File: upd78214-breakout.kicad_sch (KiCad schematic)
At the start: 1 part

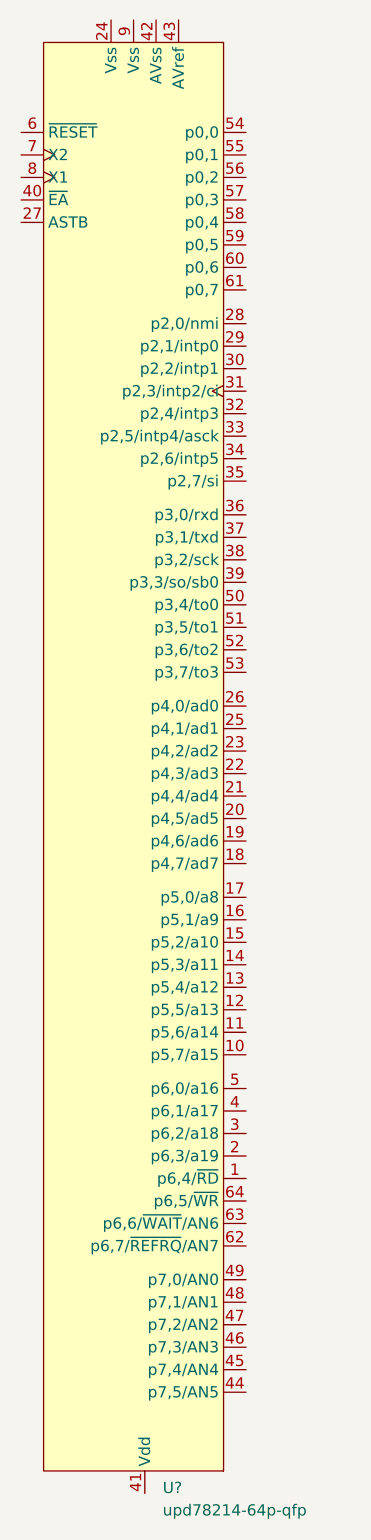
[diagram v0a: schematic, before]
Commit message: Fix VSS/VDD confusion
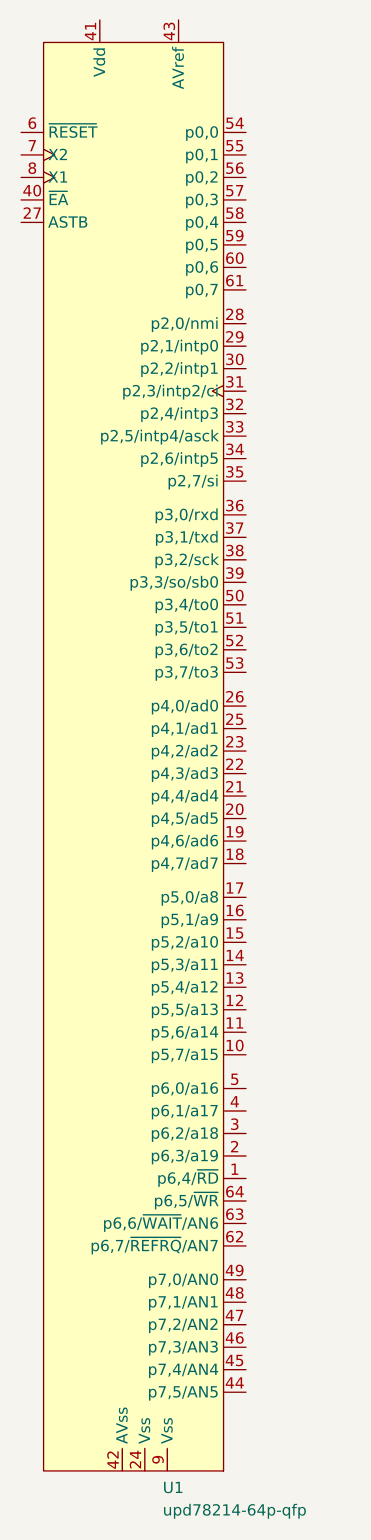
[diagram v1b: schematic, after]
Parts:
- gave numbers to parts that had none: 1
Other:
- moved on the sheet: U1
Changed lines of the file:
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@@
   (symbol (lib_id "NEC:upd78214-64p-qfp") (at 121.285 26.035 0) (unit 1)
     (in_bom yes) (on_board yes) (fields_autoplaced)
-    (property "Reference" "U?" (id 0) (at 123.3044 187.96 0)
+    (property "Reference" "U1" (id 0) (at 123.3044 187.96 0)
       (effects (font (size 1.27 1.27)) (justify left))
     )
@@
   (symbol_instances
     (path "/69c7afce-fa24-4138-9624-1d45a5afe81a"
-      (reference "U?") (unit 1) (value "upd78214-64p-qfp") (footprint "Package_QFP:TQFP-64_14x14mm_P0.8mm")
+      (reference "U1") (unit 1) (value "upd78214-64p-qfp") (footprint "Package_QFP:TQFP-64_14x14mm_P0.8mm")
     )
   )

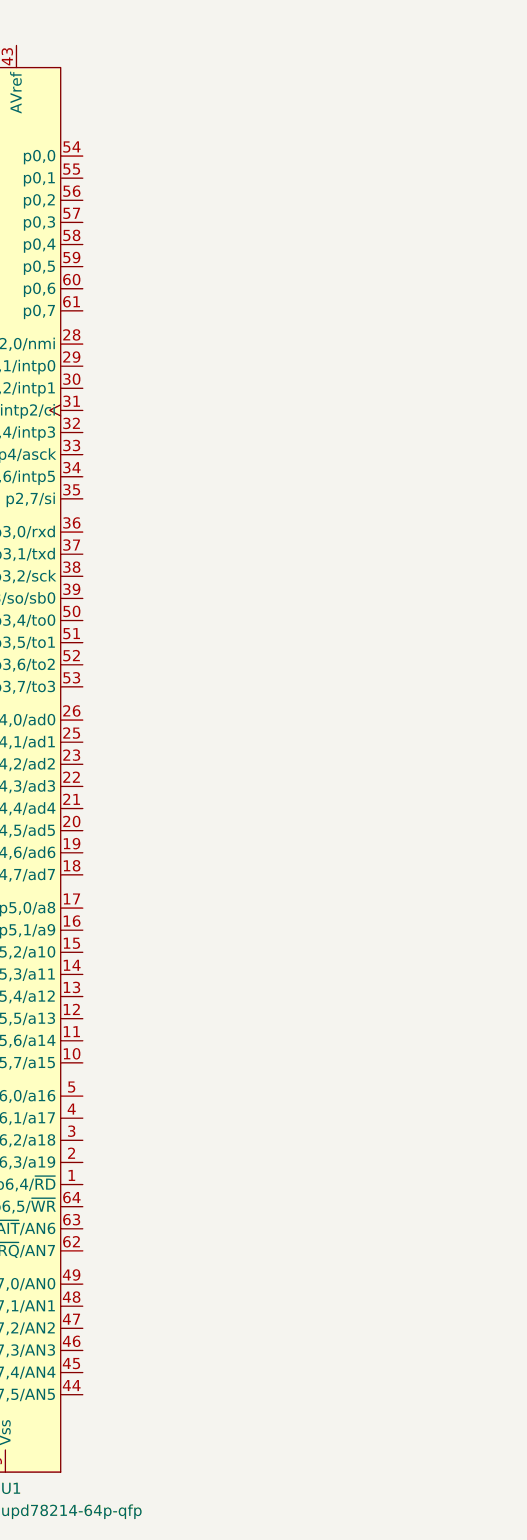
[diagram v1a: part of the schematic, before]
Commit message: NEC footprint, Toshiba symbol
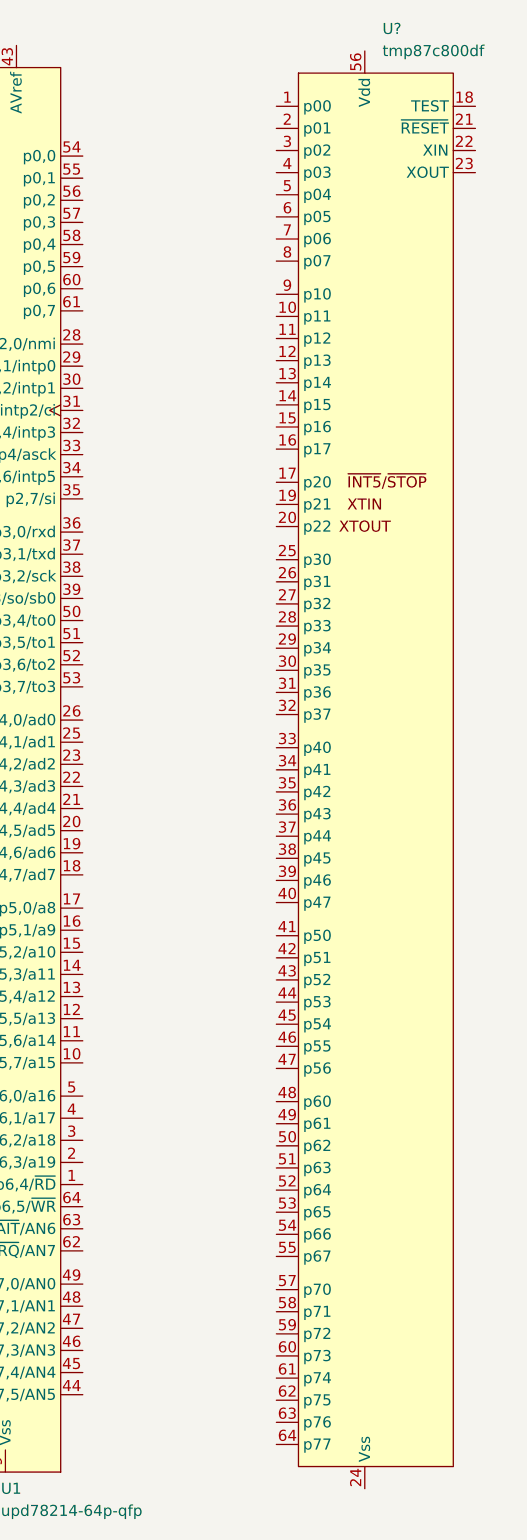
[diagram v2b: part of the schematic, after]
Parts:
- added U?: tmp87c800df, symbol Toshiba:tmp87c800df
- U1: footprint Package_QFP:TQFP-64_14x14mm_P0.8mm -> NEC:QFP-64_14x14_Pitch0.8mm
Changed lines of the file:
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@@
       (effects (font (size 1.27 1.27)) (justify left))
     )
-    (property "Footprint" "Package_QFP:TQFP-64_14x14mm_P0.8mm" (id 2) (at 121.285 26.035 0)
+    (property "Footprint" "NEC:QFP-64_14x14_Pitch0.8mm" (id 2) (at 121.285 26.035 0)
       (effects (font (size 1.27 1.27)) hide)
     )
     (property "Datasheet" "" (id 3) (at 121.285 26.035 0)
+      (effects (font (size 1.27 1.27)) hide)
+    )
+    (pin "1")
+    (pin "10")
+    (pin "11")
+    (pin "12")
+    (pin "13")
+    (pin "14")
+    (pin "15")
+    (pin "16")
+    (pin "17")
+    (pin "18")
+    (pin "19")
+    (pin "2")
+    (pin "20")
+    (pin "21")
+    (pin "22")
+    (pin "23")
+    (pin "24")
+    (pin "25")
+    (pin "26")
+    (pin "27")
+    (pin "28")
+    (pin "29")
+    (pin "3")
+    (pin "30")
+    (pin "31")
+    (pin "32")
+    (pin "33")
+    (pin "34")
+    (pin "35")
+    (pin "36")
+    (pin "37")
+    (pin "38")
+    (pin "39")
+    (pin "4")
+    (pin "40")
+    (pin "41")
+    (pin "42")
+    (pin "43")
+    (pin "44")
+    (pin "45")
+    (pin "46")
+    (pin "47")
+    (pin "48")
+    (pin "49")
+    (pin "5")
+    (pin "50")
+    (pin "51")
+    (pin "52")
+    (pin "53")
+    (pin "54")
+    (pin "55")
+    (pin "56")
+    (pin "57")
+    (pin "58")
+    (pin "59")
+    (pin "6")
+    (pin "60")
+    (pin "61")
+    (pin "62")
+    (pin "63")
+    (pin "64")
+    (pin "7")
+    (pin "8")
+    (pin "9")
+  )
+  (symbol (lib_id "Toshiba:tmp87c800df") (at 170.18 38.1 0) (unit 1)
+    (in_bom yes) (on_board yes) (fields_autoplaced)
+    (property "Reference" "U?" (id 0) (at 167.1194 20.32 0)
+      (effects (font (size 1.27 1.27)) (justify left))
+    )
+    (property "Value" "tmp87c800df" (id 1) (at 167.1194 22.86 0)
+      (effects (font (size 1.27 1.27)) (justify left))
+    )
+    (property "Footprint" "" (id 2) (at 170.18 38.1 0)
+      (effects (font (size 1.27 1.27)) hide)
+    )
+    (property "Datasheet" "" (id 3) (at 170.18 38.1 0)
       (effects (font (size 1.27 1.27)) hide)
     )
@@
   (symbol_instances
     (path "/69c7afce-fa24-4138-9624-1d45a5afe81a"
-      (reference "U1") (unit 1) (value "upd78214-64p-qfp") (footprint "Package_QFP:TQFP-64_14x14mm_P0.8mm")
+      (reference "U1") (unit 1) (value "upd78214-64p-qfp") (footprint "NEC:QFP-64_14x14_Pitch0.8mm")
+    )
+    (path "/d24b5999-bb41-4238-a79a-8ddf5d237a80"
+      (reference "U?") (unit 1) (value "tmp87c800df") (footprint "")
     )
   )

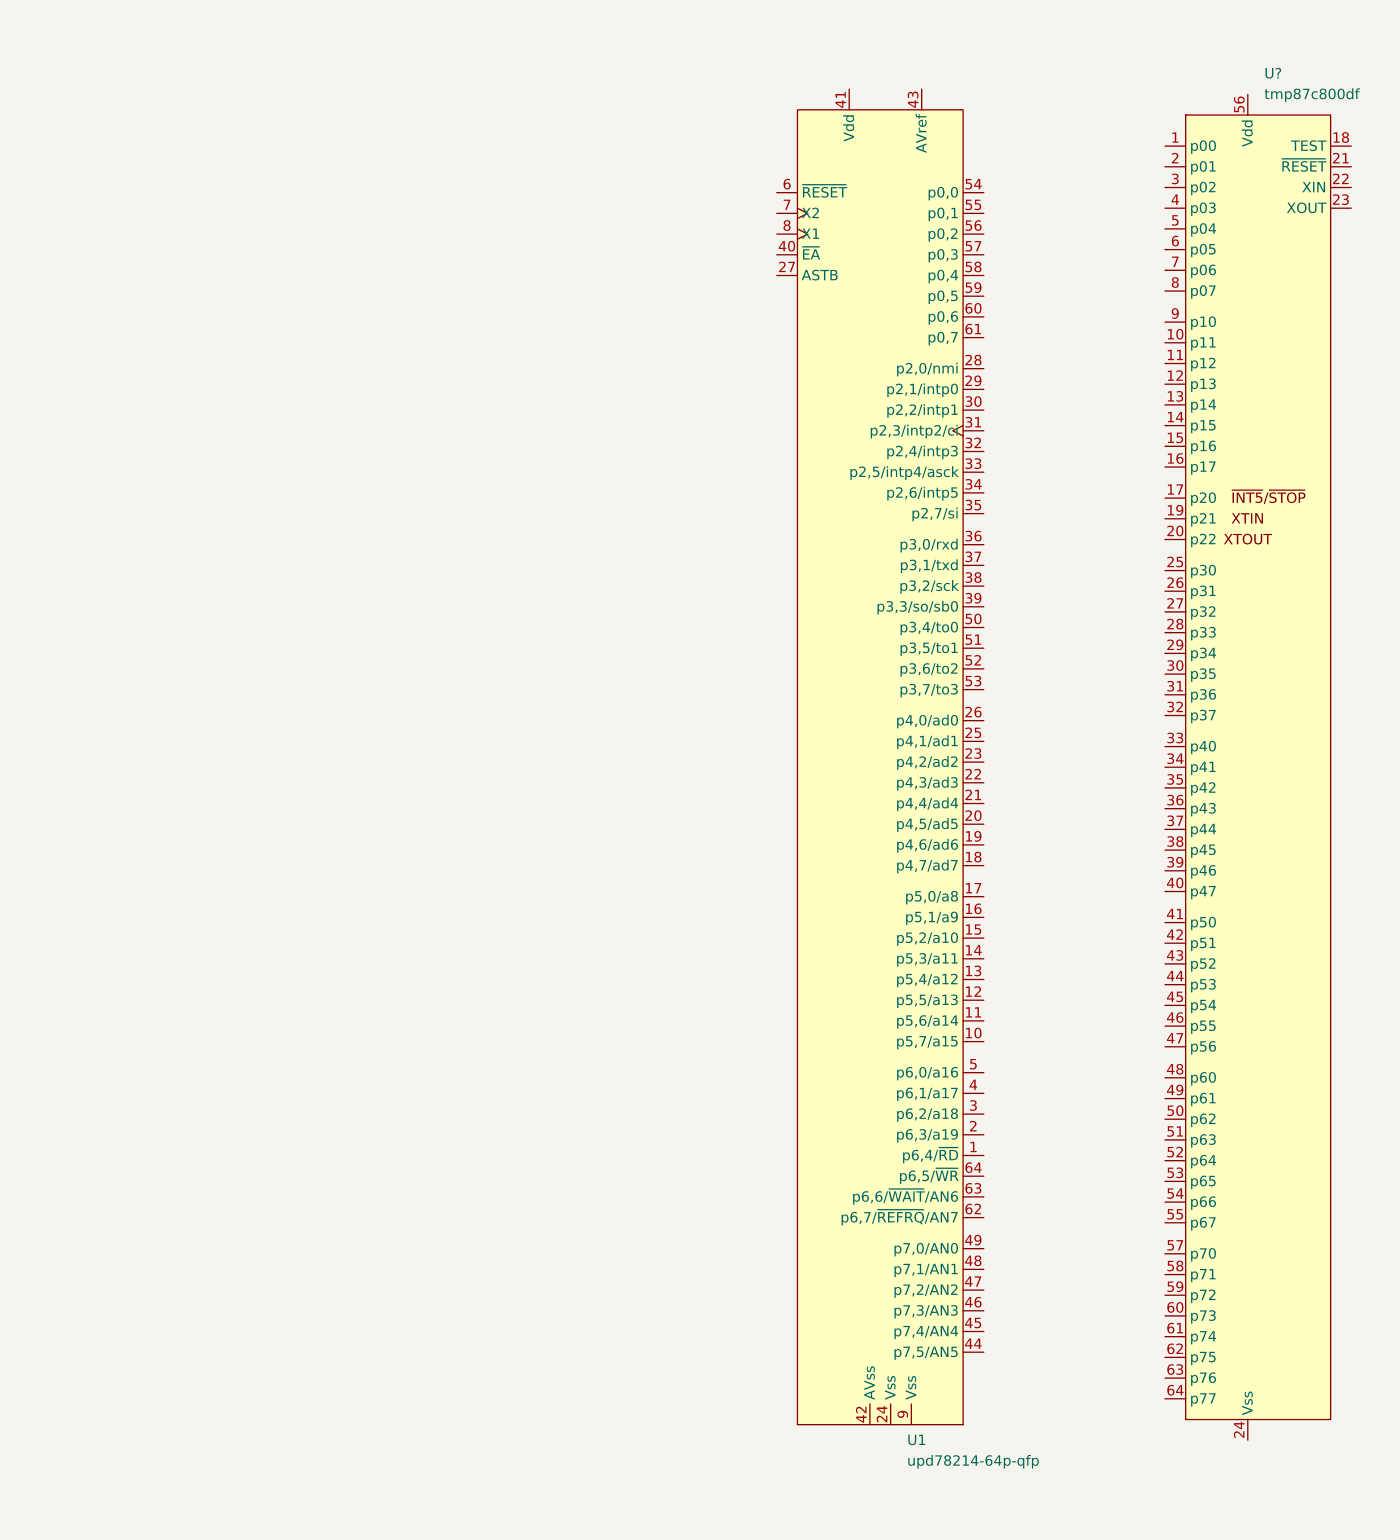
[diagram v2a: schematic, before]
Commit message: USB power for test board
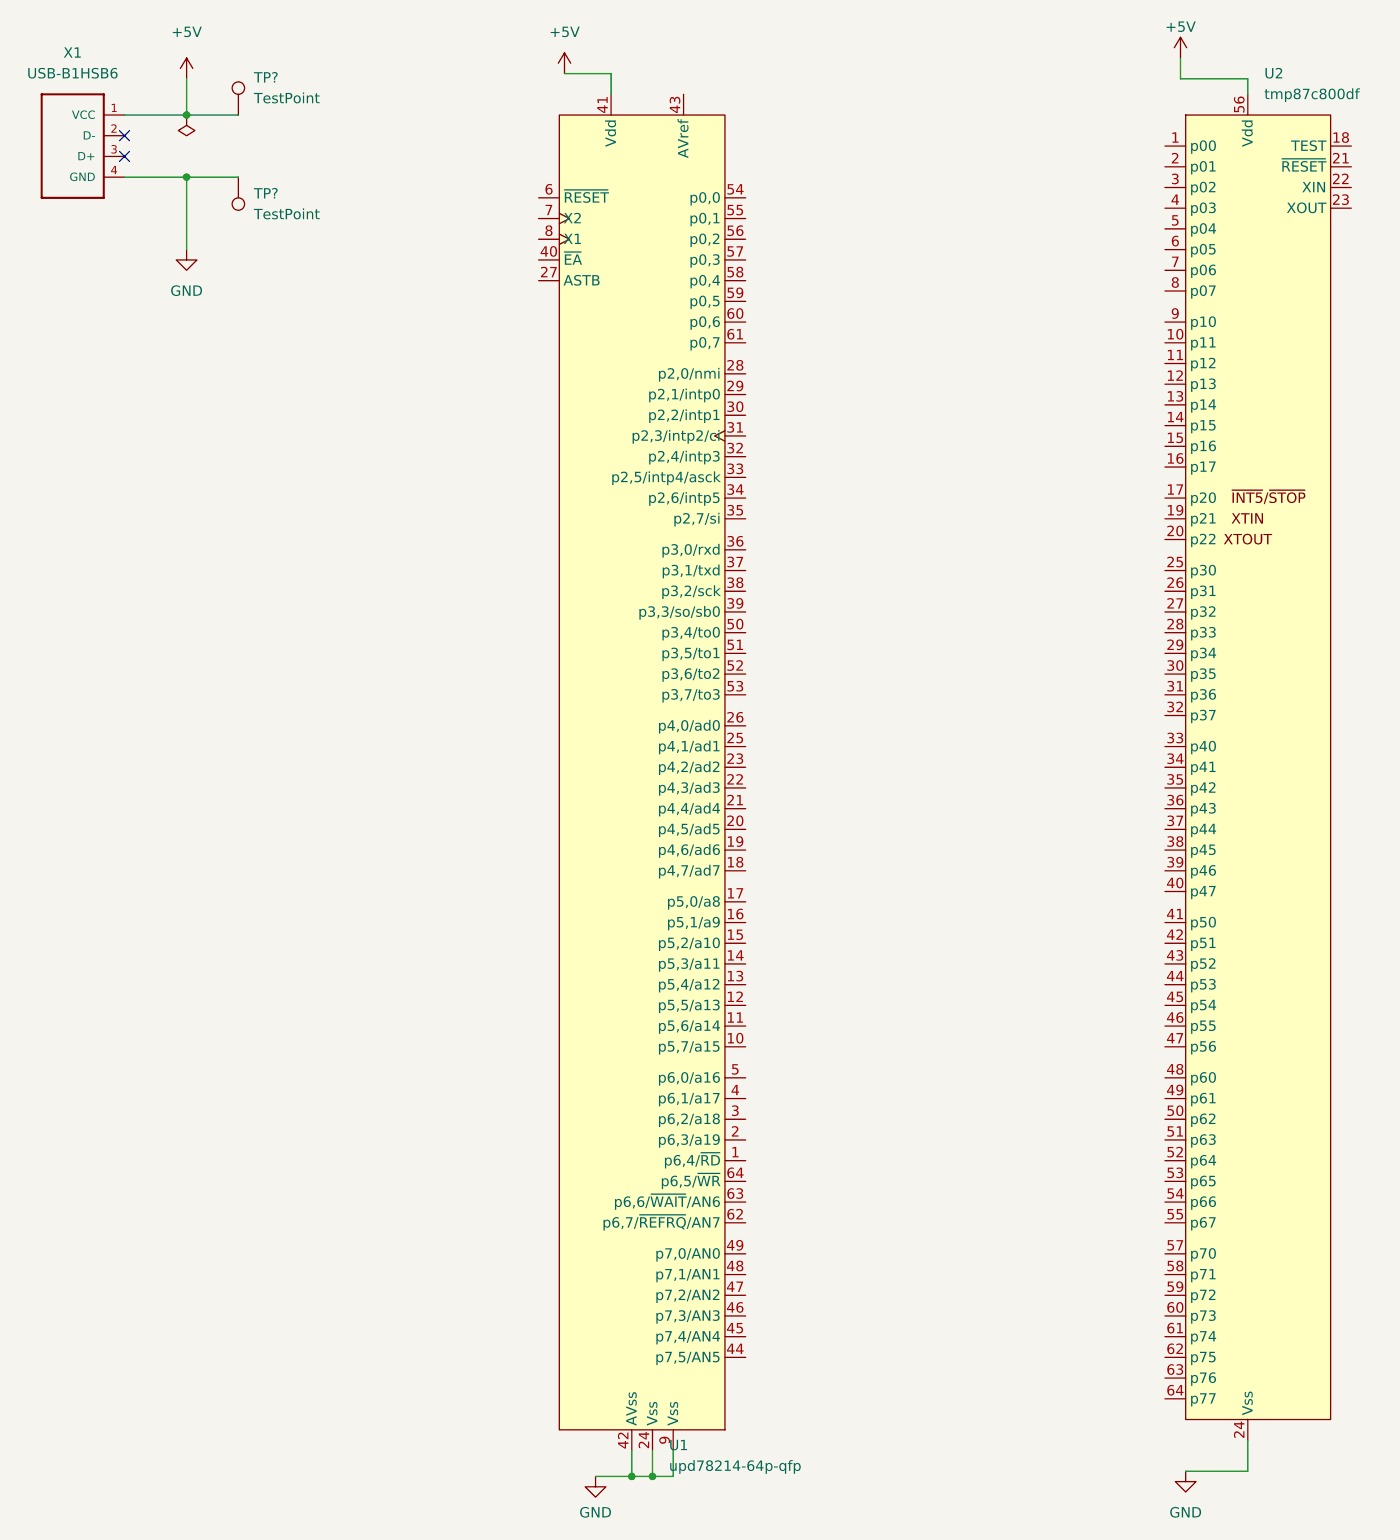
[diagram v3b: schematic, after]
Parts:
- added TP? (x2): TestPoint, TestPoint:TestPoint_Loop_D2.50mm_Drill1.0mm, symbol Connector:TestPoint
- added X1: USB-B1HSB6, OST_USB-B1HSB6, symbol USB-B1HSB6-2:USB-B1HSB6
- U2: renamed from U?; footprint (none) -> NEC:QFP-64_14x14_Pitch0.8mm
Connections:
- net GND: now reaches U1.24 (Vss)
- net GND: now also U1.42 (AVss), U1.9 (Vss), U2.24 (Vss), TP?.1, X1.4 (GND)
- net +5V: now reaches U1.41 (Vdd)
- net +5V: now also U2.56 (Vdd), TP?.1, X1.1 (VCC)
- no-connect marks 0 -> 2
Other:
- moved on the sheet: U1
